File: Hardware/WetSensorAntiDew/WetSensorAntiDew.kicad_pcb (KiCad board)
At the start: 2 copper layers, 38.1 x 48.8 mm, 30 parts, among them J2 Connector to BME280, J3 4P4C, J5 Connector to power supply, J6 Conn_01x04_Socket, J8 6P6C, Q1 MOSFET N-CH, SW1 SW_Push, U1 AMS1117, U3 STM32F103C6Tx, Y1 Crystal_GND24_Small

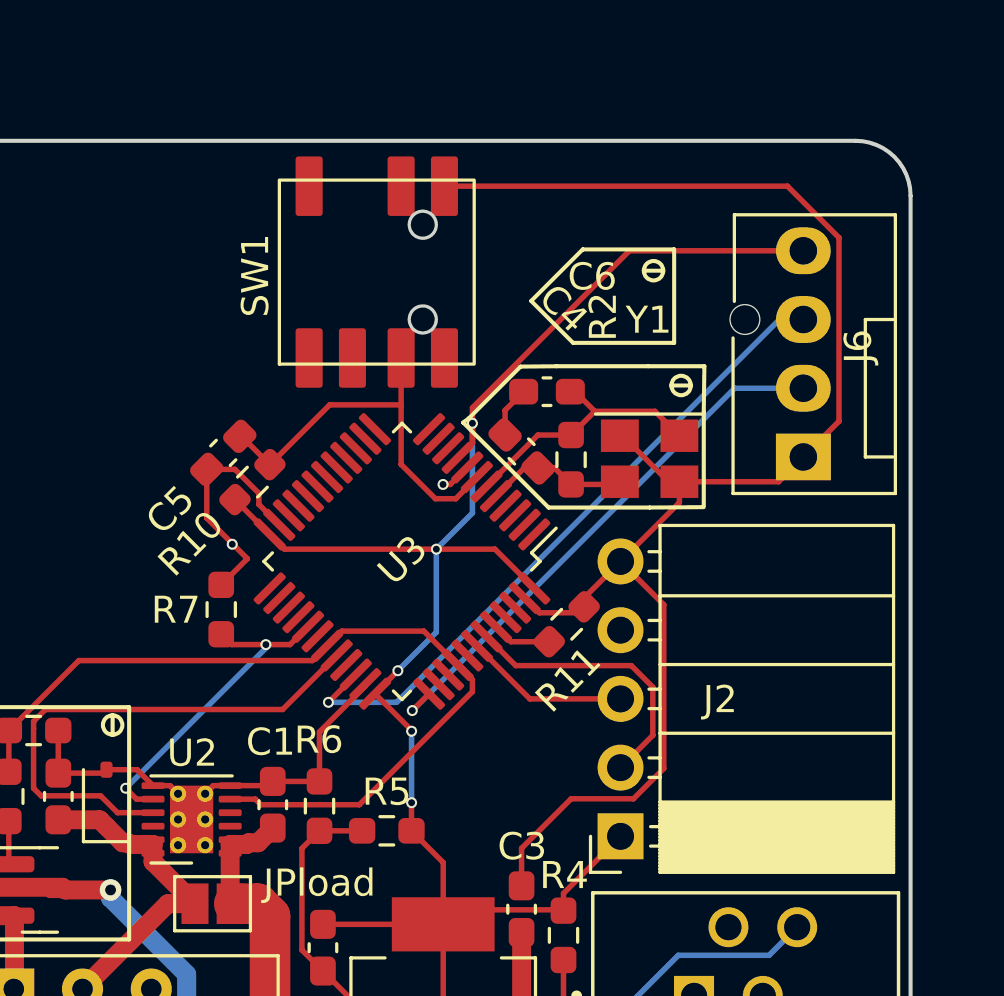
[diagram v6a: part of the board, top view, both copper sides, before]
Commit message: small edits to DRC Check pass
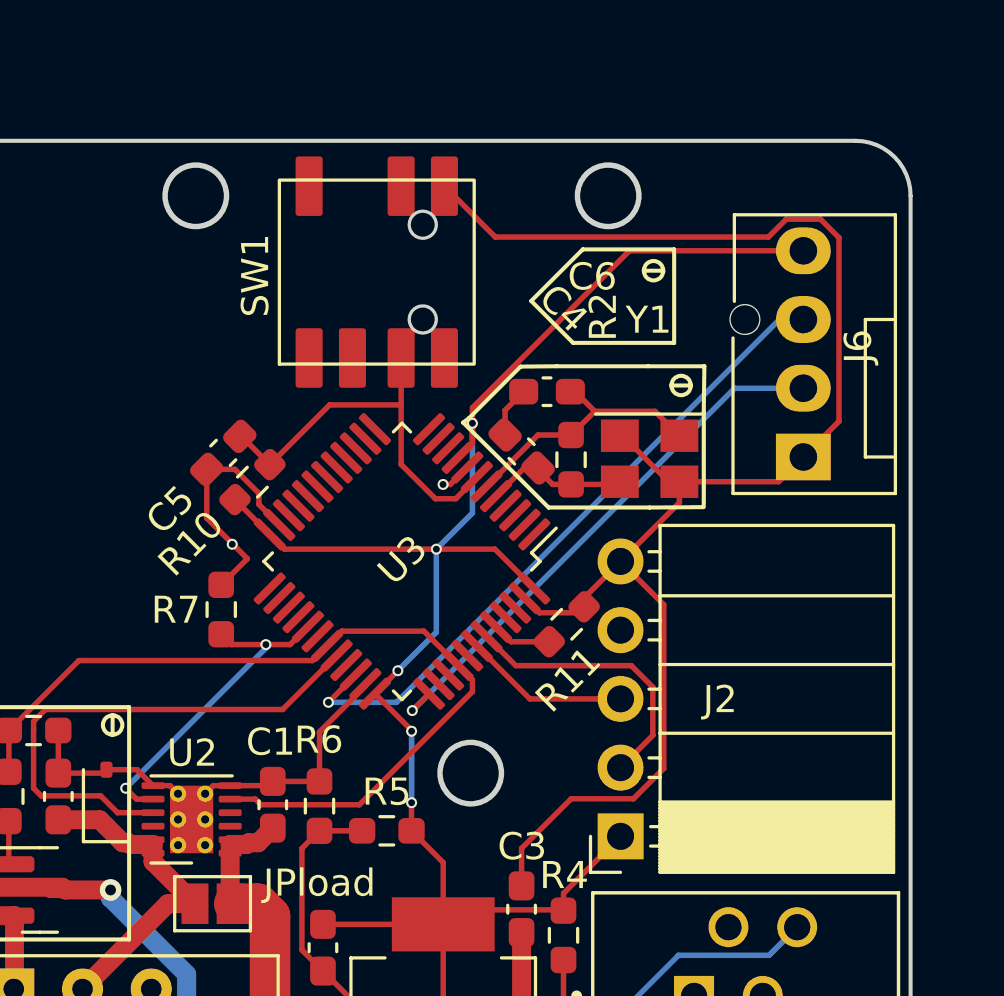
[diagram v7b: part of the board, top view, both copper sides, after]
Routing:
- net Earth: track 87.3 -> 87.8 mm
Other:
- outline, holes or cut-outs redrawn
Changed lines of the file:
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@@
     )
   )
-  (gr_rect (start 96.79605 114.037424) (end 100.94715 109.3904)
+  (gr_rect (start 96.79605 109.3904) (end 100.94715 114.037424)
     (stroke (width 0.15) (type default)) (fill none) (layer "B.SilkS"))
   (gr_line (start 97.5 110.35921) (end 97.5 109.64079)
@@
   (gr_line (start 128.016 86.36) (end 93.98 86.36)
     (stroke (width 0.15) (type default)) (layer "Edge.Cuts"))
+  (gr_circle (center 118.872 88.392) (end 120.007923 88.392)
+    (stroke (width 0.2) (type default)) (fill none) (layer "Edge.Cuts"))
   (gr_line (start 93.98 135.128) (end 128.016 135.128)
     (stroke (width 0.15) (type default)) (layer "Edge.Cuts"))
@@
   (gr_arc (start 128.016 86.36) (mid 129.45284 86.955159) (end 130.048 88.392)
     (stroke (width 0.15) (type default)) (layer "Edge.Cuts"))
+  (gr_circle (center 103.632 88.392) (end 104.767923 88.392)
+    (stroke (width 0.2) (type default)) (fill none) (layer "Edge.Cuts"))
+  (gr_circle (center 113.792 109.728) (end 114.927923 109.728)
+    (stroke (width 0.2) (type default)) (fill none) (layer "Edge.Cuts"))
   (gr_arc (start 91.948 88.392) (mid 92.543159 86.95516) (end 93.98 86.36)
     (stroke (width 0.15) (type default)) (layer "Edge.Cuts"))
@@
   (segment (start 109.899658 106.507572) (end 108.204 108.20323) (width 0.2032) (layer "F.Cu") (net 2))
   (segment (start 104.902 110.19) (end 104.277 110.19) (width 0.2032) (layer "F.Cu") (net 2))
-  (segment (start 127.4022 89.940778) (end 127.4022 96.7274) (width 0.2032) (layer "F.Cu") (net 2))
+  (segment (start 127.4022 96.7274) (end 126.0856 98.044) (width 0.2032) (layer "F.Cu") (net 2))
   (segment (start 104.03784 100.303946) (end 104.9782 101.244306) (width 0.2032) (layer "F.Cu") (net 2))
+  (segment (start 114.700031 89.916) (end 124.793778 89.916) (width 0.2032) (layer "F.Cu") (net 2))
   (segment (start 115.6716 112.507809) (end 117.503009 110.6764) (width 0.2032) (layer "F.Cu") (net 2))
   (segment (start 120.9262 103.5018) (end 119.3292 101.9048) (width 0.2032) (layer "F.Cu") (net 2))
-  (segment (start 127.4022 96.7274) (end 126.0856 98.044) (width 0.2032) (layer "F.Cu") (net 2))
   (segment (start 102.977 110.49) (end 102.677 110.19) (width 0.2032) (layer "F.Cu") (net 2))
   (segment (start 100.203 109.728) (end 100.33 109.601) (width 0.2032) (layer "F.Cu") (net 2))
+  (segment (start 125.452378 89.2574) (end 126.718822 89.2574) (width 0.2032) (layer "F.Cu") (net 2))
   (segment (start 120.9262 109.556409) (end 120.9262 103.5018) (width 0.2032) (layer "F.Cu") (net 2))
   (segment (start 119.3038 97.2584) (end 119.4038 97.2584) (width 0.2032) (layer "F.Cu") (net 2))
@@
   (segment (start 117.503009 110.6764) (end 119.806209 110.6764) (width 0.2032) (layer "F.Cu") (net 2))
   (segment (start 105.963615 99.798395) (end 105.963615 99.386659) (width 0.2032) (layer "F.Cu") (net 2))
+  (segment (start 126.718822 89.2574) (end 127.4022 89.940778) (width 0.2032) (layer "F.Cu") (net 2))
   (segment (start 117.983 103.5812) (end 117.983 103.251) (width 0.2032) (layer "F.Cu") (net 2))
   (segment (start 106.717678 100.552458) (end 105.963615 99.798395) (width 0.2032) (layer "F.Cu") (net 2))
@@
   (segment (start 121.5038 99.7302) (end 121.5038 98.9584) (width 0.2032) (layer "F.Cu") (net 2))
   (segment (start 106.3207 110.19) (end 106.4768 110.0339) (width 0.2032) (layer "F.Cu") (net 2))
+  (segment (start 127.4022 89.940778) (end 127.4022 96.7274) (width 0.2032) (layer "F.Cu") (net 2))
   (segment (start 117.983 103.5812) (end 117.762521 103.801679) (width 0.2032) (layer "F.Cu") (net 2))
-  (segment (start 112.820431 88.0364) (end 125.497822 88.0364) (width 0.2032) (layer "F.Cu") (net 2))
+  (segment (start 112.820431 88.0364) (end 114.700031 89.916) (width 0.2032) (layer "F.Cu") (net 2))
+  (segment (start 124.793778 89.916) (end 125.452378 89.2574) (width 0.2032) (layer "F.Cu") (net 2))
   (segment (start 102.677 110.19) (end 102.052 110.19) (width 0.2032) (layer "F.Cu") (net 2))
   (segment (start 104.902 110.19) (end 106.3207 110.19) (width 0.2032) (layer "F.Cu") (net 2))
@@
   (segment (start 113.665002 98.431138) (end 113.036531 99.059609) (width 0.2032) (layer "F.Cu") (net 2))
   (segment (start 104.277 110.19) (end 103.977 110.49) (width 0.2032) (layer "F.Cu") (net 2))
-  (segment (start 125.497822 88.0364) (end 127.4022 89.940778) (width 0.2032) (layer "F.Cu") (net 2))
   (segment (start 121.1038 98.9584) (end 121.5038 98.9584) (width 0.2032) (layer "F.Cu") (net 2))
   (segment (start 98.5501 108.1532) (end 98.5501 109.7261) (width 0.2032) (layer "F.Cu") (net 2))
@@
   (segment (start 113.3125 114.7795) (end 117.1906 114.7795) (width 0.2032) (layer "F.Cu") (net 5))
   (segment (start 113.855986 97.533048) (end 113.855986 96.224011) (width 0.2032) (layer "F.Cu") (net 5))
+  (segment (start 111.6038 110.824) (end 111.6076 110.8202) (width 0.2032) (layer "F.Cu") (net 5))
   (segment (start 112.522 101.450549) (end 114.686837 101.450549) (width 0.2032) (layer "F.Cu") (net 5))
+  (segment (start 117.1906 114.7795) (end 117.221 114.8099) (width 0.2032) (layer "F.Cu") (net 5))
   (segment (start 112.776 113.0319) (end 111.6038 111.8597) (width 0.2032) (layer "F.Cu") (net 5))
-  (segment (start 111.6038 110.824) (end 111.6076 110.8202) (width 0.2032) (layer "F.Cu") (net 5))
-  (segment (start 117.1906 114.7795) (end 117.221 114.8099) (width 0.2032) (layer "F.Cu") (net 5))
   (segment (start 106.364124 100.906012) (end 106.908661 101.450549) (width 0.2032) (layer "F.Cu") (net 5))
   (segment (start 112.776 118.872) (end 112.776 115.316) (width 0.2032) (layer "F.Cu") (net 5))
@@
   (segment (start 113.855986 96.224011) (end 119.655997 90.424) (width 0.2032) (layer "F.Cu") (net 5))
   (segment (start 111.6076 108.147064) (end 110.253212 106.792676) (width 0.2032) (layer "F.Cu") (net 5))
-  (segment (start 111.76 111.7035) (end 111.6038 111.8597) (width 0.2032) (layer "F.Cu") (net 5))
   (segment (start 113.311449 98.077585) (end 113.855986 97.533048) (width 0.2032) (layer "F.Cu") (net 5))
   (segment (start 112.776 121.616) (end 112.776 118.872) (width 0.2032) (layer "F.Cu") (net 5))
@@
   (segment (start 111.0996 105.9434) (end 111.0996 105.946288) (width 0.2032) (layer "F.Cu") (net 5))
   (segment (start 105.0798 99.6188) (end 105.0798 99.621688) (width 0.2032) (layer "F.Cu") (net 5))
+  (segment (start 119.655997 90.424) (end 126.0856 90.424) (width 0.2032) (layer "F.Cu") (net 5))
   (segment (start 112.776 115.316) (end 112.776 113.0319) (width 0.2032) (layer "F.Cu") (net 5))
-  (segment (start 119.655997 90.424) (end 126.0856 90.424) (width 0.2032) (layer "F.Cu") (net 5))
   (segment (start 111.0996 105.946288) (end 110.253212 106.792676) (width 0.2032) (layer "F.Cu") (net 5))
   (segment (start 111.6076 108.1786) (end 111.6076 108.147064) (width 0.2032) (layer "F.Cu") (net 5))
@@
   (segment (start 96.7232 112.8882) (end 96.931 113.096) (width 0.2032) (layer "F.Cu") (net 12))
   (segment (start 96.7232 111.5022) (end 96.7232 112.8882) (width 0.2032) (layer "F.Cu") (net 12))
+  (segment (start 115.76678 98.45068) (end 116.28148 98.45068) (width 0.2032) (layer "F.Cu") (net 13))
+  (segment (start 116.818258 99.0581) (end 117.5004 99.0581) (width 0.2032) (layer "F.Cu") (net 13))
+  (segment (start 116.28148 98.45068) (end 116.28148 98.521322) (width 0.2032) (layer "F.Cu") (net 13))
+  (segment (start 116.28148 98.521322) (end 116.818258 99.0581) (width 0.2032) (layer "F.Cu") (net 13))
+  (segment (start 117.5004 99.0581) (end 119.2041 99.0581) (width 0.2032) (layer "F.Cu") (net 13))
   (segment (start 119.2041 99.0581) (end 119.3038 98.9584) (width 0.2032) (layer "F.Cu") (net 13))
-  (segment (start 117.5004 99.0581) (end 119.2041 99.0581) (width 0.2032) (layer "F.Cu") (net 13))
-  (segment (start 116.28148 98.45068) (end 116.89298 98.45068) (width 0.2032) (layer "F.Cu") (net 13))
-  (segment (start 116.89298 98.45068) (end 117.5004 99.0581) (width 0.2032) (layer "F.Cu") (net 13))
-  (segment (start 115.76678 98.45068) (end 116.28148 98.45068) (width 0.2032) (layer "F.Cu") (net 13))
-  (segment (start 119.3038 98.9584) (end 119.29266 98.94726) (width 0.2032) (layer "F.Cu") (net 13))
   (segment (start 114.725662 99.491798) (end 115.76678 98.45068) (width 0.2032) (layer "F.Cu") (net 13))
   (segment (start 115.06172 96.31818) (end 115.7489 95.631) (width 0.2032) (layer "F.Cu") (net 18))
@@
   (segment (start 97.6376 107.815797) (end 97.6376 108.077) (width 0.2032) (layer "F.Cu") (net 53))
   (zone (net 2) (net_name "Earth") (layer "B.Cu") (hatch edge 0.5)
-    (connect_pads (clearance 0.1778))
+    (connect_pads thru_hole_only (clearance 0.1778))
     (min_thickness 0.25) (filled_areas_thickness no)
     (fill yes (thermal_gap 0.5) (thermal_bridge_width 0.5))

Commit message: edited switch and programming pins connections
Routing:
- net Earth: track 87.8 -> 80.6 mm
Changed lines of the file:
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@@
   (segment (start 109.899658 106.507572) (end 108.204 108.20323) (width 0.2032) (layer "F.Cu") (net 2))
   (segment (start 104.902 110.19) (end 104.277 110.19) (width 0.2032) (layer "F.Cu") (net 2))
-  (segment (start 127.4022 96.7274) (end 126.0856 98.044) (width 0.2032) (layer "F.Cu") (net 2))
   (segment (start 104.03784 100.303946) (end 104.9782 101.244306) (width 0.2032) (layer "F.Cu") (net 2))
-  (segment (start 114.700031 89.916) (end 124.793778 89.916) (width 0.2032) (layer "F.Cu") (net 2))
   (segment (start 115.6716 112.507809) (end 117.503009 110.6764) (width 0.2032) (layer "F.Cu") (net 2))
   (segment (start 120.9262 103.5018) (end 119.3292 101.9048) (width 0.2032) (layer "F.Cu") (net 2))
   (segment (start 102.977 110.49) (end 102.677 110.19) (width 0.2032) (layer "F.Cu") (net 2))
   (segment (start 100.203 109.728) (end 100.33 109.601) (width 0.2032) (layer "F.Cu") (net 2))
-  (segment (start 125.452378 89.2574) (end 126.718822 89.2574) (width 0.2032) (layer "F.Cu") (net 2))
+  (segment (start 112.820431 88.0364) (end 114.2318 88.0364) (width 0.25) (layer "F.Cu") (net 2))
   (segment (start 120.9262 109.556409) (end 120.9262 103.5018) (width 0.2032) (layer "F.Cu") (net 2))
   (segment (start 119.3038 97.2584) (end 119.4038 97.2584) (width 0.2032) (layer "F.Cu") (net 2))
+  (segment (start 124.2394 98.044) (end 126.0856 98.044) (width 0.25) (layer "F.Cu") (net 2))
   (segment (start 109.899658 106.439122) (end 109.899658 106.507572) (width 0.2032) (layer "F.Cu") (net 2))
   (segment (start 105.963615 99.386659) (end 105.078716 98.50176) (width 0.2032) (layer "F.Cu") (net 2))
@@
   (segment (start 117.503009 110.6764) (end 119.806209 110.6764) (width 0.2032) (layer "F.Cu") (net 2))
   (segment (start 105.963615 99.798395) (end 105.963615 99.386659) (width 0.2032) (layer "F.Cu") (net 2))
-  (segment (start 126.718822 89.2574) (end 127.4022 89.940778) (width 0.2032) (layer "F.Cu") (net 2))
   (segment (start 117.983 103.5812) (end 117.983 103.251) (width 0.2032) (layer "F.Cu") (net 2))
   (segment (start 106.717678 100.552458) (end 105.963615 99.798395) (width 0.2032) (layer "F.Cu") (net 2))
@@
   (segment (start 121.5038 99.7302) (end 121.5038 98.9584) (width 0.2032) (layer "F.Cu") (net 2))
   (segment (start 106.3207 110.19) (end 106.4768 110.0339) (width 0.2032) (layer "F.Cu") (net 2))
-  (segment (start 127.4022 89.940778) (end 127.4022 96.7274) (width 0.2032) (layer "F.Cu") (net 2))
   (segment (start 117.983 103.5812) (end 117.762521 103.801679) (width 0.2032) (layer "F.Cu") (net 2))
-  (segment (start 112.820431 88.0364) (end 114.700031 89.916) (width 0.2032) (layer "F.Cu") (net 2))
-  (segment (start 124.793778 89.916) (end 125.452378 89.2574) (width 0.2032) (layer "F.Cu") (net 2))
   (segment (start 102.677 110.19) (end 102.052 110.19) (width 0.2032) (layer "F.Cu") (net 2))
   (segment (start 104.902 110.19) (end 106.3207 110.19) (width 0.2032) (layer "F.Cu") (net 2))
   (segment (start 125.1712 98.9584) (end 126.0856 98.044) (width 0.2032) (layer "F.Cu") (net 2))
+  (segment (start 114.2318 88.0364) (end 124.2394 98.044) (width 0.25) (layer "F.Cu") (net 2))
   (segment (start 119.4038 97.2584) (end 121.1038 98.9584) (width 0.2032) (layer "F.Cu") (net 2))
   (segment (start 113.036531 99.059609) (end 112.769108 99.059609) (width 0.2032) (layer "F.Cu") (net 2))
@@
   (segment (start 114.686837 101.450549) (end 116.139876 102.903588) (width 0.2032) (layer "F.Cu") (net 5))
   (segment (start 113.3125 114.7795) (end 117.1906 114.7795) (width 0.2032) (layer "F.Cu") (net 5))
-  (segment (start 113.855986 97.533048) (end 113.855986 96.224011) (width 0.2032) (layer "F.Cu") (net 5))
   (segment (start 111.6038 110.824) (end 111.6076 110.8202) (width 0.2032) (layer "F.Cu") (net 5))
   (segment (start 112.522 101.450549) (end 114.686837 101.450549) (width 0.2032) (layer "F.Cu") (net 5))
@@
   (segment (start 112.776 113.0319) (end 111.6038 111.8597) (width 0.2032) (layer "F.Cu") (net 5))
   (segment (start 106.364124 100.906012) (end 106.908661 101.450549) (width 0.2032) (layer "F.Cu") (net 5))
+  (segment (start 113.855986 97.533048) (end 113.855986 96.7994) (width 0.2032) (layer "F.Cu") (net 5))
   (segment (start 112.776 118.872) (end 112.776 115.316) (width 0.2032) (layer "F.Cu") (net 5))
   (segment (start 108.331 115.3171) (end 108.3321 115.316) (width 0.2032) (layer "F.Cu") (net 5))
   (segment (start 106.908661 101.450549) (end 112.522 101.450549) (width 0.2032) (layer "F.Cu") (net 5))
-  (segment (start 113.855986 96.224011) (end 119.655997 90.424) (width 0.2032) (layer "F.Cu") (net 5))
   (segment (start 111.6076 108.147064) (end 110.253212 106.792676) (width 0.2032) (layer "F.Cu") (net 5))
   (segment (start 113.311449 98.077585) (end 113.855986 97.533048) (width 0.2032) (layer "F.Cu") (net 5))
@@
   (segment (start 111.0996 105.9434) (end 111.0996 105.946288) (width 0.2032) (layer "F.Cu") (net 5))
   (segment (start 105.0798 99.6188) (end 105.0798 99.621688) (width 0.2032) (layer "F.Cu") (net 5))
-  (segment (start 119.655997 90.424) (end 126.0856 90.424) (width 0.2032) (layer "F.Cu") (net 5))
   (segment (start 112.776 115.316) (end 112.776 113.0319) (width 0.2032) (layer "F.Cu") (net 5))
   (segment (start 111.0996 105.946288) (end 110.253212 106.792676) (width 0.2032) (layer "F.Cu") (net 5))
@@
   (via (at 111.6076 108.1786) (size 0.4064) (drill 0.254) (layers "F.Cu" "B.Cu") (net 5))
   (via (at 111.0996 105.9434) (size 0.4064) (drill 0.254) (layers "F.Cu" "B.Cu") (net 5))
+  (segment (start 113.855986 96.7994) (end 118.7958 96.7994) (width 0.2032) (layer "B.Cu") (net 5))
   (segment (start 112.522 101.450549) (end 112.522 104.521) (width 0.2032) (layer "B.Cu") (net 5))
   (segment (start 113.855986 100.116563) (end 112.522 101.450549) (width 0.2032) (layer "B.Cu") (net 5))
+  (segment (start 118.7958 96.7994) (end 125.1712 90.424) (width 0.2032) (layer "B.Cu") (net 5))
+  (segment (start 125.1712 90.424) (end 126.0856 90.424) (width 0.2032) (layer "B.Cu") (net 5))
   (segment (start 113.855986 96.7994) (end 113.855986 100.116563) (width 0.2032) (layer "B.Cu") (net 5))
   (segment (start 111.6076 110.8202) (end 111.6076 108.1786) (width 0.2032) (layer "B.Cu") (net 5))
